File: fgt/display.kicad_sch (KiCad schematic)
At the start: 22 parts, among them J3 BL_Conn, Q1 BC817, U2 ERC12864

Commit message: DRC done
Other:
- title: FGT -> ${TITLE}
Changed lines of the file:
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@@
   (paper "A4")
   (title_block
-    (title "FGT")
-    (date "2022-01-04")
-    (rev "v1.1.0")
+    (title "${TITLE}")
+    (date "${DATE}")
+    (rev "${REVISION}")
     (company "Juraj Giertl")
     (comment 1 "j74a8g@gmail.com")

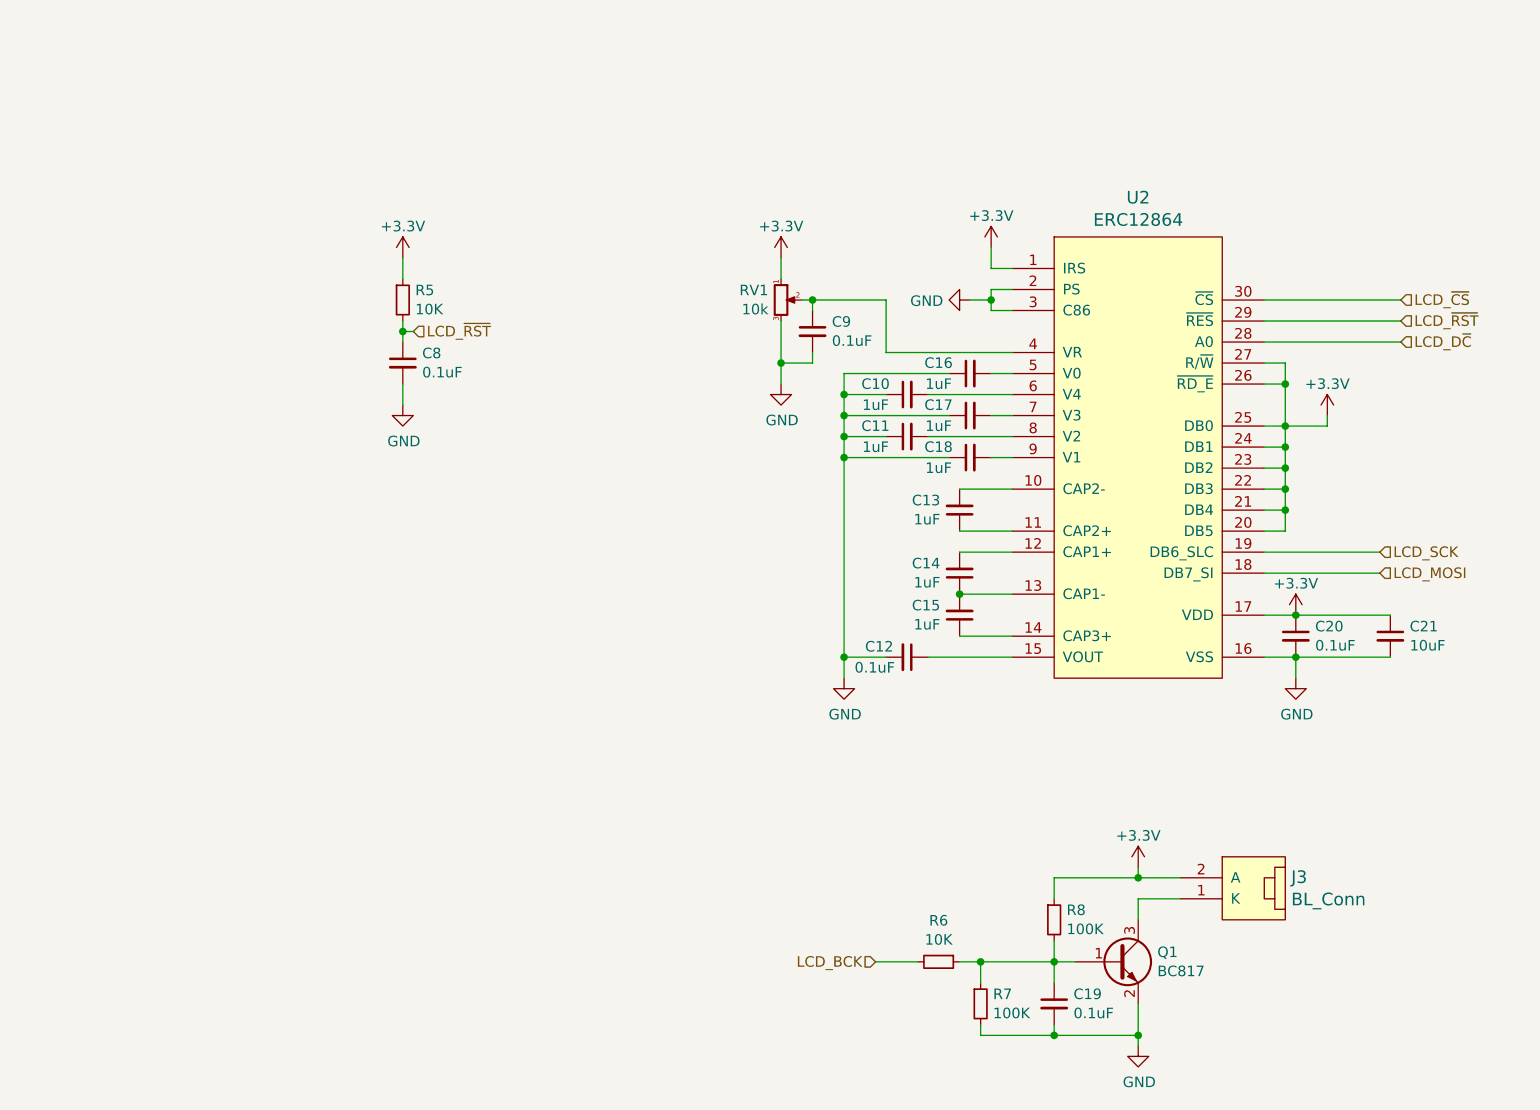
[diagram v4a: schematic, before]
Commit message: Release v1.4.0 - added testpoints - fix solder mask - size down pcb
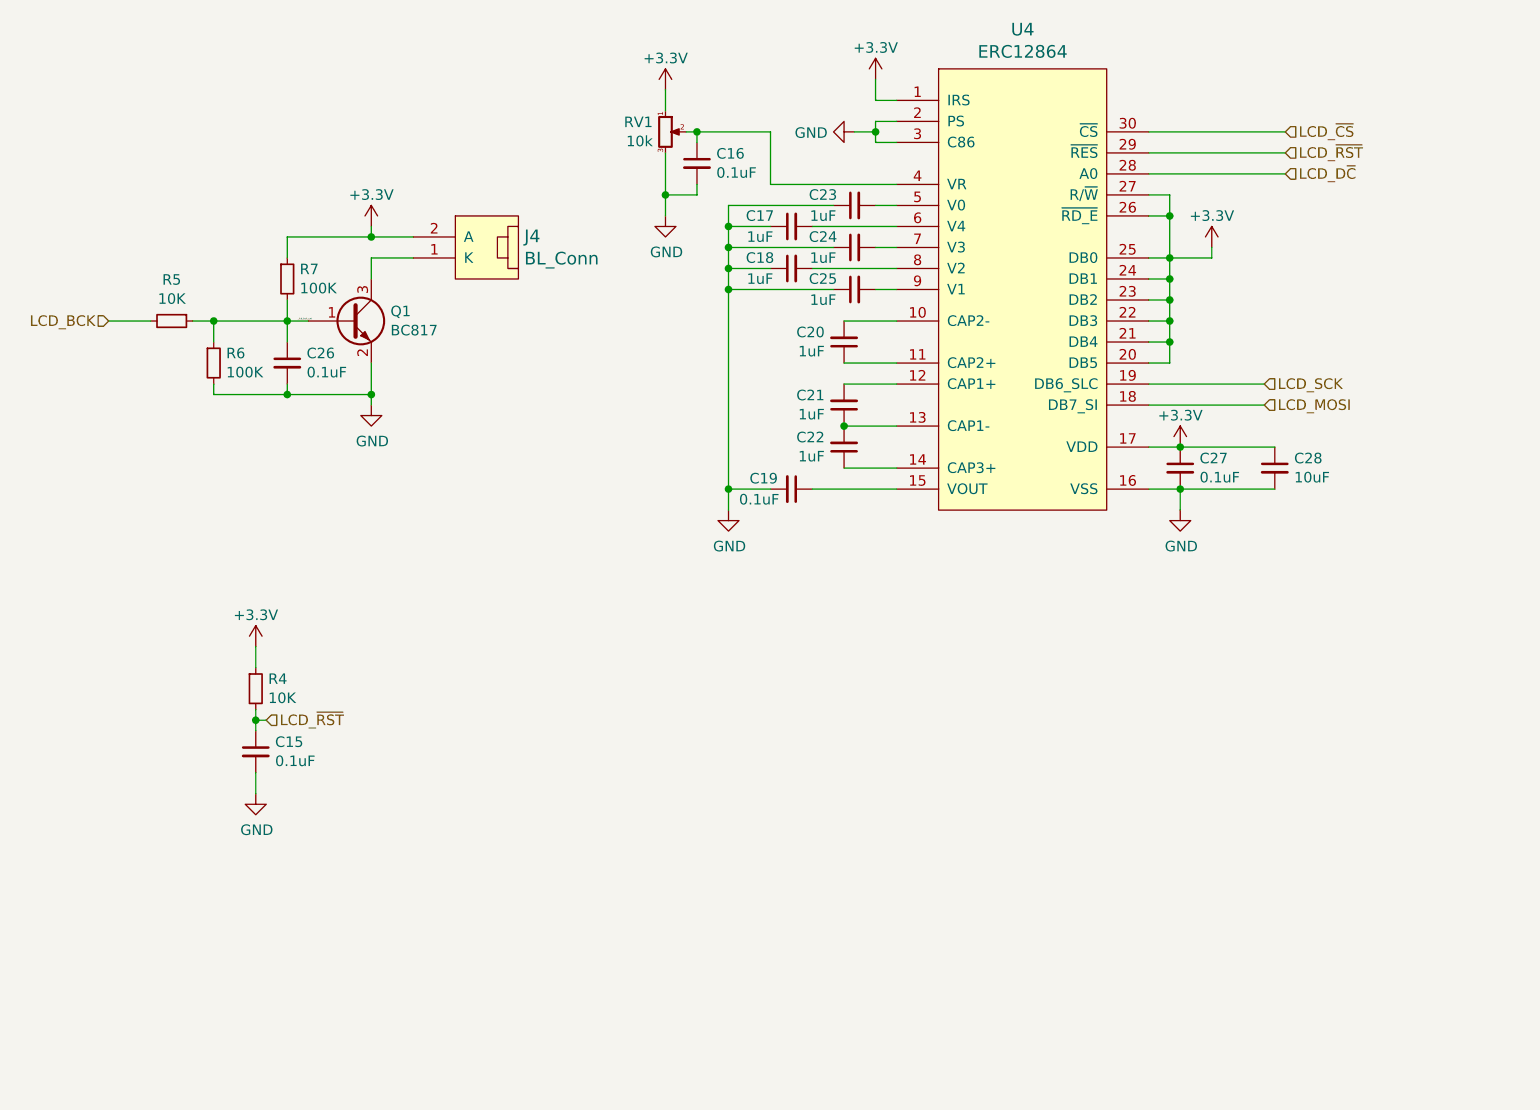
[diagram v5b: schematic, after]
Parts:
- renumbered C8 to C15, C9 to C16, C10 to C17, C11 to C18, C12 to C19, C13 to C20, C14 to C21, C15 to C22, C16 to C23, C17 to C24, C18 to C25, C19 to C26, C20 to C27, C21 to C28, J3 to J4, R5 to R4, R6 to R5, R7 to R6, R8 to R7, U2 to U4
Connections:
- net _lcd_bck_cnt: now reaches C26.1, Q1.1 (B), R5.1, R6.1, R7.2
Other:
- moved on the sheet: C15, C16, C17, C18, C19, C20, C21, C22, C23, C24, C25, C26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

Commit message: Release v1.5.0 - See changelog for changes.
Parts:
- renumbered C26 to C16, C16 to C17, C17 to C18, C18 to C19, C19 to C20, C20 to C21, C21 to C22, C22 to C23, C23 to C24, C24 to C25, C25 to C26, R5 to R4, R6 to R5, R4 to R6
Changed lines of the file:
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@@
   (symbol (lib_id "Device:R_Small") (at 48.26 105.41 0) (unit 1)
     (in_bom yes) (on_board yes)
-    (property "Reference" "R4" (id 0) (at 49.7586 104.2416 0)
+    (property "Reference" "R6" (id 0) (at 49.7586 104.2416 0)
       (effects (font (size 1.27 1.27)) (justify left))
     )
@@
   (symbol (lib_id "Device:C_Small") (at 113.03 81.28 270) (unit 1)
     (in_bom yes) (on_board yes)
-    (property "Reference" "C19" (id 0) (at 107.95 80.01 90)
+    (property "Reference" "C20" (id 0) (at 107.95 80.01 90)
       (effects (font (size 1.27 1.27)) (justify left))
     )
@@
   (symbol (lib_id "power:GND") (at 105.41 83.82 0) (unit 1)
     (in_bom yes) (on_board yes)
-    (property "Reference" "#PWR029" (id 0) (at 105.41 90.17 0)
+    (property "Reference" "#PWR031" (id 0) (at 105.41 90.17 0)
       (effects (font (size 1.27 1.27)) hide)
     )
@@
   (symbol (lib_id "Device:C_Small") (at 120.65 46.99 90) (mirror x) (unit 1)
     (in_bom yes) (on_board yes)
-    (property "Reference" "C23" (id 0) (at 116.84 45.72 90))
+    (property "Reference" "C24" (id 0) (at 116.84 45.72 90))
     (property "Value" "1uF" (id 1) (at 116.84 48.26 90))
     (property "Footprint" "Capacitor_SMD:C_0603_1608Metric" (id 2) (at 120.65 46.99 0)
@@
   (symbol (lib_id "Device:C_Small") (at 113.03 49.53 90) (mirror x) (unit 1)
     (in_bom yes) (on_board yes)
-    (property "Reference" "C17" (id 0) (at 109.22 48.26 90))
+    (property "Reference" "C18" (id 0) (at 109.22 48.26 90))
     (property "Value" "1uF" (id 1) (at 109.22 50.8 90))
     (property "Footprint" "Capacitor_SMD:C_0603_1608Metric" (id 2) (at 113.03 49.53 0)
@@
   (symbol (lib_id "Device:C_Small") (at 120.65 52.07 90) (mirror x) (unit 1)
     (in_bom yes) (on_board yes)
-    (property "Reference" "C24" (id 0) (at 116.84 50.8 90))
+    (property "Reference" "C25" (id 0) (at 116.84 50.8 90))
     (property "Value" "1uF" (id 1) (at 116.84 53.34 90))
     (property "Footprint" "Capacitor_SMD:C_0603_1608Metric" (id 2) (at 120.65 52.07 0)
@@
   (symbol (lib_id "Device:C_Small") (at 113.03 54.61 90) (mirror x) (unit 1)
     (in_bom yes) (on_board yes)
-    (property "Reference" "C18" (id 0) (at 109.22 53.34 90))
+    (property "Reference" "C19" (id 0) (at 109.22 53.34 90))
     (property "Value" "1uF" (id 1) (at 109.22 55.88 90))
     (property "Footprint" "Capacitor_SMD:C_0603_1608Metric" (id 2) (at 113.03 54.61 0)
@@
   (symbol (lib_id "Device:C_Small") (at 120.65 57.15 90) (mirror x) (unit 1)
     (in_bom yes) (on_board yes)
-    (property "Reference" "C25" (id 0) (at 116.84 55.88 90))
+    (property "Reference" "C26" (id 0) (at 116.84 55.88 90))
     (property "Value" "1uF" (id 1) (at 116.84 58.42 90))
     (property "Footprint" "Capacitor_SMD:C_0603_1608Metric" (id 2) (at 120.65 57.15 0)
@@
   (symbol (lib_id "Device:C_Small") (at 119.38 63.5 0) (mirror x) (unit 1)
     (in_bom yes) (on_board yes)
-    (property "Reference" "C20" (id 0) (at 117.0432 62.3316 0)
+    (property "Reference" "C21" (id 0) (at 117.0432 62.3316 0)
       (effects (font (size 1.27 1.27)) (justify right))
     )
@@
   (symbol (lib_id "Device:C_Small") (at 119.38 71.12 0) (mirror x) (unit 1)
     (in_bom yes) (on_board yes)
-    (property "Reference" "C21" (id 0) (at 117.0432 69.9516 0)
+    (property "Reference" "C22" (id 0) (at 117.0432 69.9516 0)
       (effects (font (size 1.27 1.27)) (justify right))
     )
@@
   (symbol (lib_id "Device:C_Small") (at 119.38 76.2 0) (mirror x) (unit 1)
     (in_bom yes) (on_board yes)
-    (property "Reference" "C22" (id 0) (at 117.0432 75.0316 0)
+    (property "Reference" "C23" (id 0) (at 117.0432 75.0316 0)
       (effects (font (size 1.27 1.27)) (justify right))
     )
@@
   (symbol (lib_id "power:+3.3V") (at 123.19 31.75 0) (unit 1)
     (in_bom yes) (on_board yes)
-    (property "Reference" "#PWR031" (id 0) (at 123.19 35.56 0)
+    (property "Reference" "#PWR033" (id 0) (at 123.19 35.56 0)
       (effects (font (size 1.27 1.27)) hide)
     )
@@
   (symbol (lib_id "power:GND") (at 120.65 38.1 270) (unit 1)
     (in_bom yes) (on_board yes)
-    (property "Reference" "#PWR030" (id 0) (at 114.3 38.1 0)
+    (property "Reference" "#PWR032" (id 0) (at 114.3 38.1 0)
       (effects (font (size 1.27 1.27)) hide)
     )
@@
   (symbol (lib_id "Device:C_Small") (at 101.6 41.91 0) (unit 1)
     (in_bom yes) (on_board yes)
-    (property "Reference" "C16" (id 0) (at 103.9368 40.7416 0)
+    (property "Reference" "C17" (id 0) (at 103.9368 40.7416 0)
       (effects (font (size 1.27 1.27)) (justify left))
     )
@@
   (symbol (lib_id "power:GND") (at 97.79 48.26 0) (unit 1)
     (in_bom yes) (on_board yes)
-    (property "Reference" "#PWR028" (id 0) (at 97.79 54.61 0)
+    (property "Reference" "#PWR030" (id 0) (at 97.79 54.61 0)
       (effects (font (size 1.27 1.27)) hide)
     )
@@
   (symbol (lib_id "power:+3.3V") (at 97.79 33.02 0) (unit 1)
     (in_bom yes) (on_board yes)
-    (property "Reference" "#PWR027" (id 0) (at 97.79 36.83 0)
+    (property "Reference" "#PWR029" (id 0) (at 97.79 36.83 0)
       (effects (font (size 1.27 1.27)) hide)
     )
@@
   (symbol (lib_id "power:+3.3V") (at 62.23 49.53 0) (unit 1)
     (in_bom yes) (on_board yes)
-    (property "Reference" "#PWR032" (id 0) (at 62.23 53.34 0)
+    (property "Reference" "#PWR027" (id 0) (at 62.23 53.34 0)
       (effects (font (size 1.27 1.27)) hide)
     )
@@
   (symbol (lib_id "power:GND") (at 62.23 71.12 0) (unit 1)
     (in_bom yes) (on_board yes)
-    (property "Reference" "#PWR033" (id 0) (at 62.23 77.47 0)
+    (property "Reference" "#PWR028" (id 0) (at 62.23 77.47 0)
       (effects (font (size 1.27 1.27)) hide)
     )
@@
   (symbol (lib_id "Device:R_Small") (at 43.18 66.04 0) (unit 1)
     (in_bom yes) (on_board yes)
-    (property "Reference" "R6" (id 0) (at 44.6786 64.8716 0)
+    (property "Reference" "R5" (id 0) (at 44.6786 64.8716 0)
       (effects (font (size 1.27 1.27)) (justify left))
     )
@@
   (symbol (lib_id "Device:C_Small") (at 52.07 66.04 0) (unit 1)
     (in_bom yes) (on_board yes)
-    (property "Reference" "C26" (id 0) (at 54.4068 64.8716 0)
+    (property "Reference" "C16" (id 0) (at 54.4068 64.8716 0)
       (effects (font (size 1.27 1.27)) (justify left))
     )
@@
   (symbol (lib_id "Device:R_Small") (at 38.1 60.96 270) (unit 1)
     (in_bom yes) (on_board yes)
-    (property "Reference" "R5" (id 0) (at 38.1 55.9816 90))
+    (property "Reference" "R4" (id 0) (at 38.1 55.9816 90))
     (property "Value" "10K" (id 1) (at 38.1 58.293 90))
     (property "Footprint" "Resistor_SMD:R_0805_2012Metric" (id 2) (at 38.1 60.96 0)
